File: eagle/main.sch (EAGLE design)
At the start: 17 parts, among them T1 2N2222, T2 2N2222, T3 2N2222

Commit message: [ update ] main.sch, simulation notes
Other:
- note added: "LTSPICE simulation results"
- note added: "VCC is 9v unreg supply"
- note added: "duty = 0.31s"
- note added: "peak current = 122mA"
- note added: "period = 0.78s"
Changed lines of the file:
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@@
 <sheet>
 <plain>
+<text x="0" y="30.48" size="1.778" layer="97">VCC is 9v unreg supply</text>
+<text x="0" y="43.18" size="1.778" layer="97">LTSPICE simulation results</text>
+<text x="0" y="40.64" size="1.778" layer="97">period = 0.78s</text>
+<text x="0" y="38.1" size="1.778" layer="97">duty = 0.31s</text>
+<text x="0" y="35.56" size="1.778" layer="97">peak current = 122mA</text>
 </plain>
 <instances>

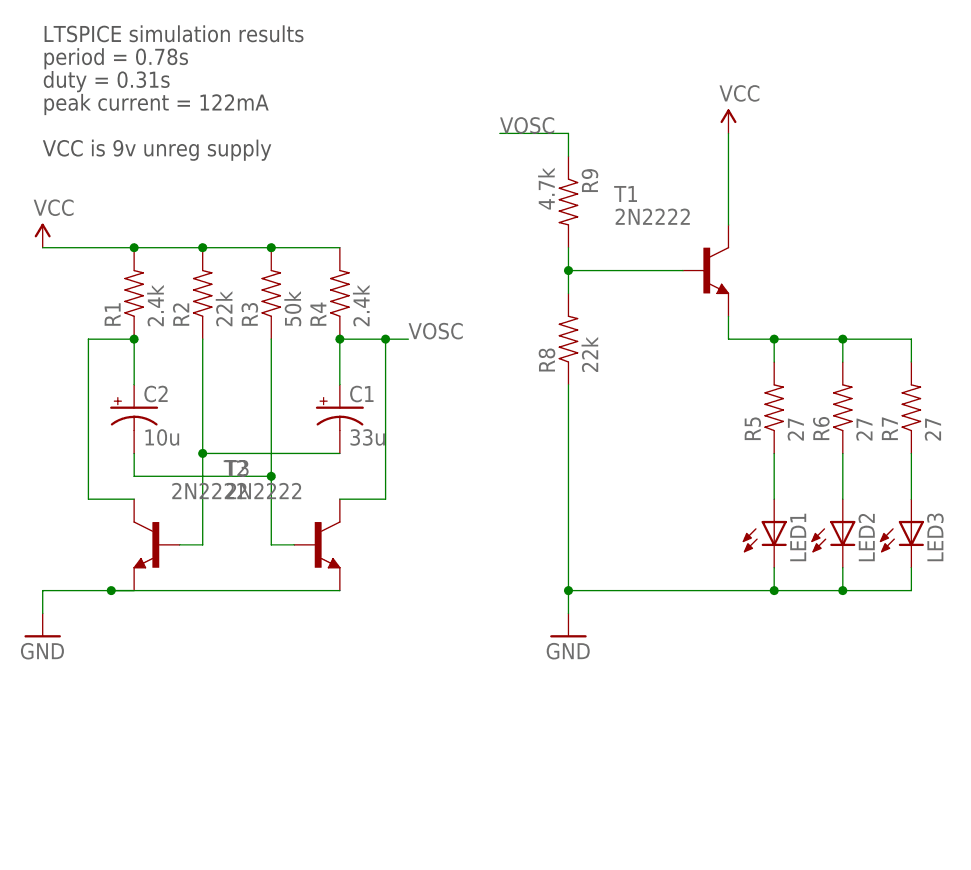
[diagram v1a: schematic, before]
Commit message: [ update ] main.sch, add connector
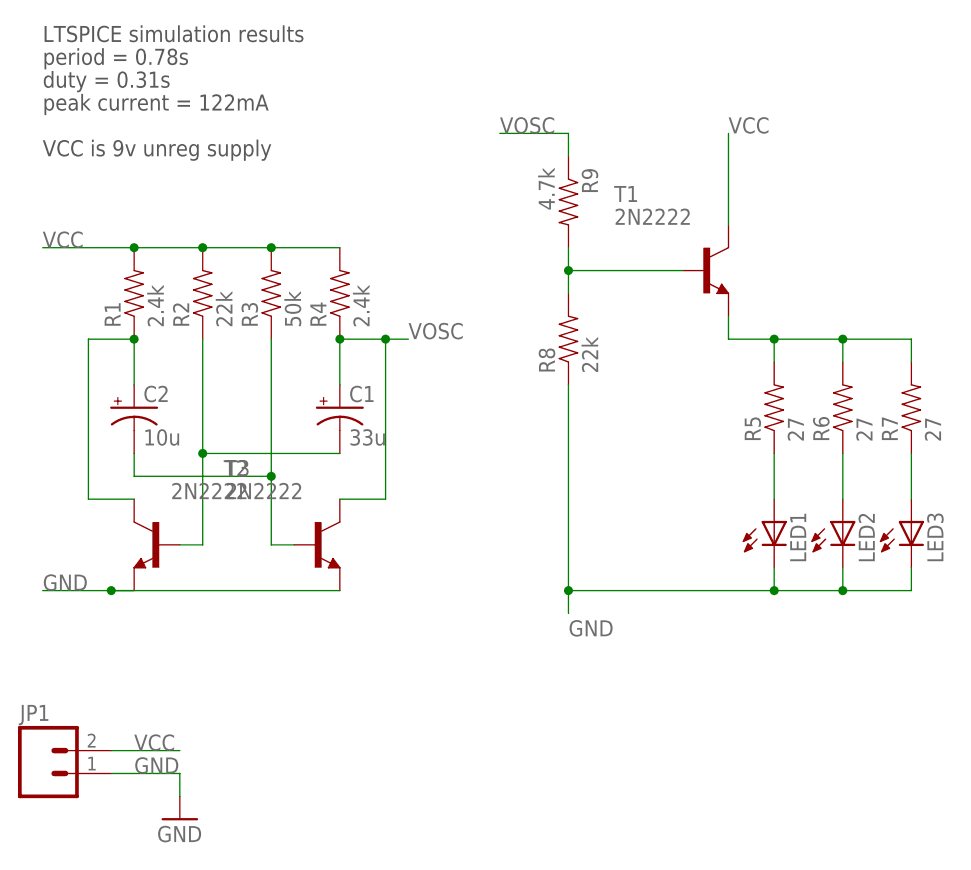
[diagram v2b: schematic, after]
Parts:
- added JP1: (no value), SparkFun:M02LOCK
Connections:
- net GND: now also JP1.1
- net VCC: now also JP1.2
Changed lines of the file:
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@@
 <part name="R8" library="SparkFun" deviceset="RESISTOR" device="PTH-1/4W" value="22k"/>
 <part name="R9" library="SparkFun" deviceset="RESISTOR" device="PTH-1/4W" value="4.7k"/>
-<part name="GND1" library="SparkFun" deviceset="GND" device=""/>
-<part name="P+1" library="SparkFun" deviceset="VCC" device=""/>
-<part name="GND2" library="SparkFun" deviceset="GND" device=""/>
 <part name="LED1" library="SparkFun" deviceset="LED" device="5MM"/>
 <part name="LED2" library="SparkFun" deviceset="LED" device="5MM"/>
 <part name="LED3" library="SparkFun" deviceset="LED" device="5MM"/>
-<part name="P+2" library="SparkFun" deviceset="VCC" device=""/>
+<part name="JP1" library="SparkFun" deviceset="M02" device="LOCK"/>
+<part name="GND3" library="SparkFun" deviceset="GND" device=""/>
 </parts>
 <sheets>
@@
 <instance part="R8" gate="G$1" x="58.42" y="10.16" rot="R90"/>
 <instance part="R9" gate="G$1" x="58.42" y="25.4" rot="R270"/>
-<instance part="GND1" gate="1" x="0" y="-22.86"/>
-<instance part="P+1" gate="1" x="0" y="20.32"/>
-<instance part="GND2" gate="1" x="58.42" y="-22.86"/>
 <instance part="LED1" gate="G$1" x="81.28" y="-10.16"/>
 <instance part="LED2" gate="G$1" x="88.9" y="-10.16"/>
 <instance part="LED3" gate="G$1" x="96.52" y="-10.16"/>
-<instance part="P+2" gate="1" x="76.2" y="33.02"/>
+<instance part="JP1" gate="G$1" x="0" y="-38.1"/>
+<instance part="GND3" gate="1" x="15.24" y="-43.18"/>
 </instances>
 <busses>
@@
 <net name="VCC" class="0">
 <segment>
-<pinref part="P+1" gate="1" pin="VCC"/>
+<pinref part="JP1" gate="G$1" pin="2"/>
+<wire x1="7.62" y1="-35.56" x2="15.24" y2="-35.56" width="0.1524" layer="91"/>
+<label x="10.16" y="-35.56" size="1.778" layer="95"/>
+</segment>
+<segment>
+<pinref part="T1" gate="G$1" pin="C"/>
+<wire x1="76.2" y1="33.02" x2="76.2" y2="22.86" width="0.1524" layer="91"/>
+<label x="76.2" y="33.02" size="1.778" layer="95"/>
+</segment>
+<segment>
 <pinref part="R1" gate="G$1" pin="2"/>
 <wire x1="0" y1="20.32" x2="10.16" y2="20.32" width="0.1524" layer="91"/>
@@
 <wire x1="25.4" y1="20.32" x2="33.02" y2="20.32" width="0.1524" layer="91"/>
 <junction x="25.4" y="20.32"/>
-</segment>
-<segment>
-<pinref part="P+2" gate="1" pin="VCC"/>
-<pinref part="T1" gate="G$1" pin="C"/>
-<wire x1="76.2" y1="33.02" x2="76.2" y2="22.86" width="0.1524" layer="91"/>
+<label x="0" y="20.32" size="1.778" layer="95"/>
 </segment>
 </net>
 <net name="GND" class="0">
 <segment>
-<wire x1="0" y1="-17.78" x2="7.62" y2="-17.78" width="0.1524" layer="91"/>
-<pinref part="T3" gate="G$1" pin="E"/>
-<wire x1="7.62" y1="-17.78" x2="33.02" y2="-17.78" width="0.1524" layer="91"/>
-<pinref part="T2" gate="G$1" pin="E"/>
-<wire x1="10.16" y1="-17.78" x2="7.62" y2="-17.78" width="0.1524" layer="91"/>
-<junction x="7.62" y="-17.78"/>
-<pinref part="GND1" gate="1" pin="GND"/>
-<wire x1="0" y1="-17.78" x2="0" y2="-20.32" width="0.1524" layer="91"/>
+<pinref part="JP1" gate="G$1" pin="1"/>
+<wire x1="7.62" y1="-38.1" x2="15.24" y2="-38.1" width="0.1524" layer="91"/>
+<label x="10.16" y="-38.1" size="1.778" layer="95"/>
+<pinref part="GND3" gate="1" pin="GND"/>
+<wire x1="15.24" y1="-38.1" x2="15.24" y2="-40.64" width="0.1524" layer="91"/>
 </segment>
 <segment>
 <pinref part="R8" gate="G$1" pin="1"/>
-<pinref part="GND2" gate="1" pin="GND"/>
 <wire x1="58.42" y1="5.08" x2="58.42" y2="-17.78" width="0.1524" layer="91"/>
 <wire x1="58.42" y1="-17.78" x2="58.42" y2="-20.32" width="0.1524" layer="91"/>
@@
 <wire x1="81.28" y1="-15.24" x2="81.28" y2="-17.78" width="0.1524" layer="91"/>
 <junction x="81.28" y="-17.78"/>
+<label x="58.42" y="-22.86" size="1.778" layer="95"/>
+</segment>
+<segment>
+<wire x1="0" y1="-17.78" x2="7.62" y2="-17.78" width="0.1524" layer="91"/>
+<pinref part="T3" gate="G$1" pin="E"/>
+<wire x1="7.62" y1="-17.78" x2="33.02" y2="-17.78" width="0.1524" layer="91"/>
+<pinref part="T2" gate="G$1" pin="E"/>
+<wire x1="10.16" y1="-17.78" x2="7.62" y2="-17.78" width="0.1524" layer="91"/>
+<junction x="7.62" y="-17.78"/>
+<label x="0" y="-17.78" size="1.778" layer="95"/>
 </segment>
 </net>

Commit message: [ add ] main.brd
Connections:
- new net N$42: R8.2, R9.2, T1.B
- net VOSC: no longer R8.2, R9.2, T1.B
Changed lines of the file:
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@@
-</segment>
-<segment>
-<pinref part="R9" gate="G$1" pin="2"/>
-<pinref part="R8" gate="G$1" pin="2"/>
-<wire x1="58.42" y1="20.32" x2="58.42" y2="17.78" width="0.1524" layer="91"/>
-<pinref part="T1" gate="G$1" pin="B"/>
-<wire x1="58.42" y1="17.78" x2="58.42" y2="15.24" width="0.1524" layer="91"/>
-<wire x1="58.42" y1="17.78" x2="71.12" y2="17.78" width="0.1524" layer="91"/>
-<junction x="58.42" y="17.78"/>
 </segment>
 <segment>
@@
 </segment>
 </net>
+<net name="N$42" class="0">
+<segment>
+<pinref part="R9" gate="G$1" pin="2"/>
+<pinref part="R8" gate="G$1" pin="2"/>
+<wire x1="58.42" y1="20.32" x2="58.42" y2="17.78" width="0.1524" layer="91"/>
+<pinref part="T1" gate="G$1" pin="B"/>
+<wire x1="58.42" y1="17.78" x2="58.42" y2="15.24" width="0.1524" layer="91"/>
+<wire x1="58.42" y1="17.78" x2="71.12" y2="17.78" width="0.1524" layer="91"/>
+<junction x="58.42" y="17.78"/>
+</segment>
+</net>
